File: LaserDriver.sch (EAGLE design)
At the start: 13 parts

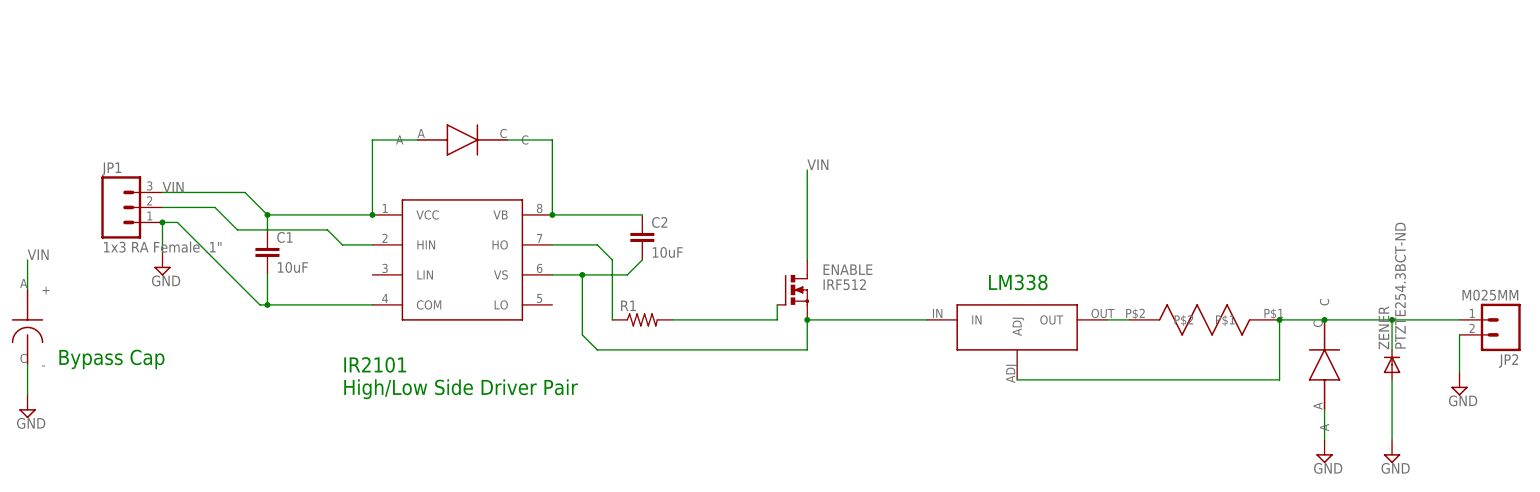
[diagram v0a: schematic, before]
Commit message: revised for capacitive loads
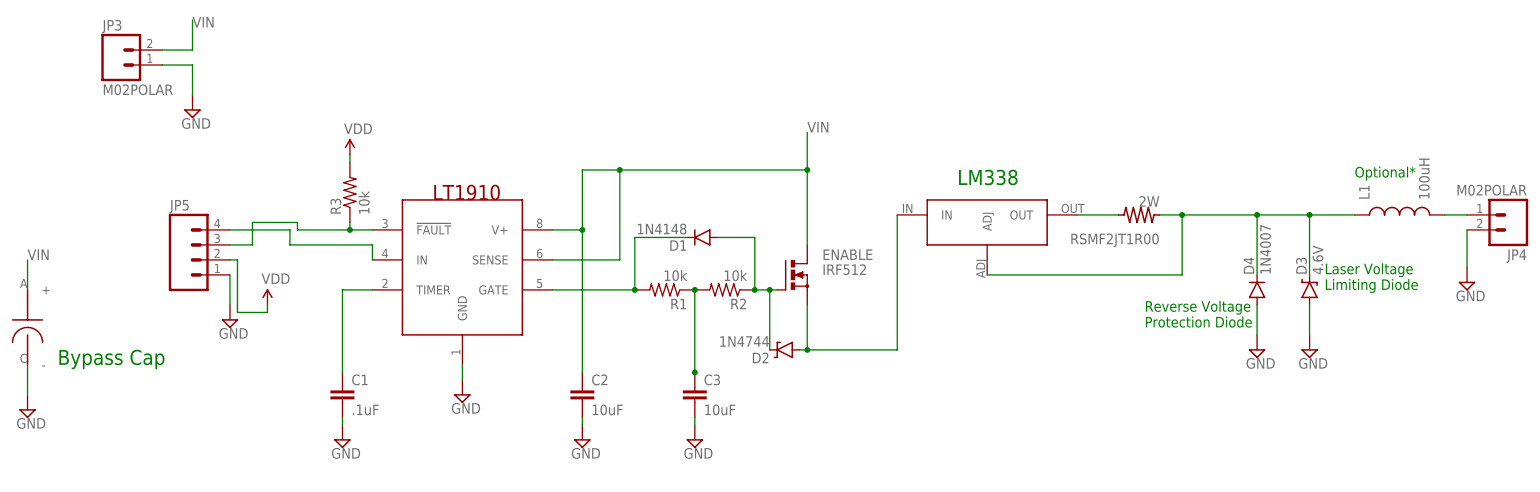
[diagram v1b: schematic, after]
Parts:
- removed DRIVER_DIODE, OVERVOLT_PROTECTION: DFLS1150, hmcfabstudio:DFLS1150
- removed JP1: 1x3 RA Female .1", SparkFun-Connectors:M03SMD_RA_FEMALE
- removed JP2: M025MM, SparkFun-Connectors:M025MM
- removed U$5: PWR_RESISTOR, hmcfabstudio:PWR_RESISTOR
- removed U$6: IR2101, hmcfabstudio:IR2101
- removed ZENER: PTZTE254.3BCT-ND, diode:DIODE-DO214AA
- added C3: 10uF, SparkFun-Capacitors:10UF-6.3V-20%(1206)
- added D1: 1N4148, SparkFun-DiscreteSemi:DIODE1N4148
- added D2: 1N4744, SparkFun-DiscreteSemi:DIODE-ZENERPTH
- added D3: 4.6V, SparkFun-DiscreteSemi:DIODE-ZENERPTH
- added D4: 1N4007, SparkFun-DiscreteSemi:DIODE
- added JP3, JP4: M02POLAR, SparkFun-Connectors:M02POLAR
- added JP5: (no value), SparkFun-Connectors:M04SMD
- added L1: 100uH, SparkFun-Passives:INDUCTORAXIAL-0.6
- added R2, R3: 10k, SparkFun-Passives:RESISTOR1206
- added RSMF2JT1R00: 2W, hmcfabstudio:PWR_RESISTOR
- added U$1: LT1910, hmcfabstudio:LT1910
- C1: value 10uF -> .1uF
- R1: value (none) -> 10k
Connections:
- removed net N$8: JP2.1, OVERVOLT_PROTECTION.C, U$2.ADJ, U$5.P$1, ZENER.C
- new net N$1: JP4.1, L1.2
- new net N$10: D1.C, R1.2, U$1.GATE
- new net N$11: D3.C, D4.C, L1.1, RSMF2JT1R00.P$1, U$2.ADJ
- new net N$3: C1.1, U$1.TIMER
- new net VDD: JP5.2, R3.2
- net GND: now also C2.2, C3.2, D3.A, D4.A, JP3.1, JP4.2, JP5.1, U$1.GND; no longer JP1.1, JP2.2, OVERVOLT_PROTECTION.A, U$6.COM, ZENER.A
- net N$2: now also JP5.3, R3.1, U$1.!FAULT!; no longer C2.1, DRIVER_DIODE.C, U$6.VB
- net N$4: now also D2.A; no longer C2.2, U$6.VS
- net N$5: now also C3.1, R2.2; no longer U$6.HO
- net N$6: now also D1.A, D2.C, R2.1; no longer R1.2
- net N$7: now also RSMF2JT1R00.P$2; no longer U$5.P$2
- net N$9: now also JP5.4, U$1.IN; no longer JP1.2, U$6.HIN
- net VIN: now also C2.1, JP3.2, U$1.SENSE, U$1.V+; no longer C1.1, DRIVER_DIODE.A, JP1.3, U$6.VCC
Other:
- note added: "Laser Voltage Limiting Diode"
- note added: "Optional*"
- note added: "Reverse Voltage Protection Diode"
- note removed: "IR2101 High/Low Side Driver Pair"
- moved on the sheet: C1, C2, ENABLE, R1
